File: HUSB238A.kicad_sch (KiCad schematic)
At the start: 1 part

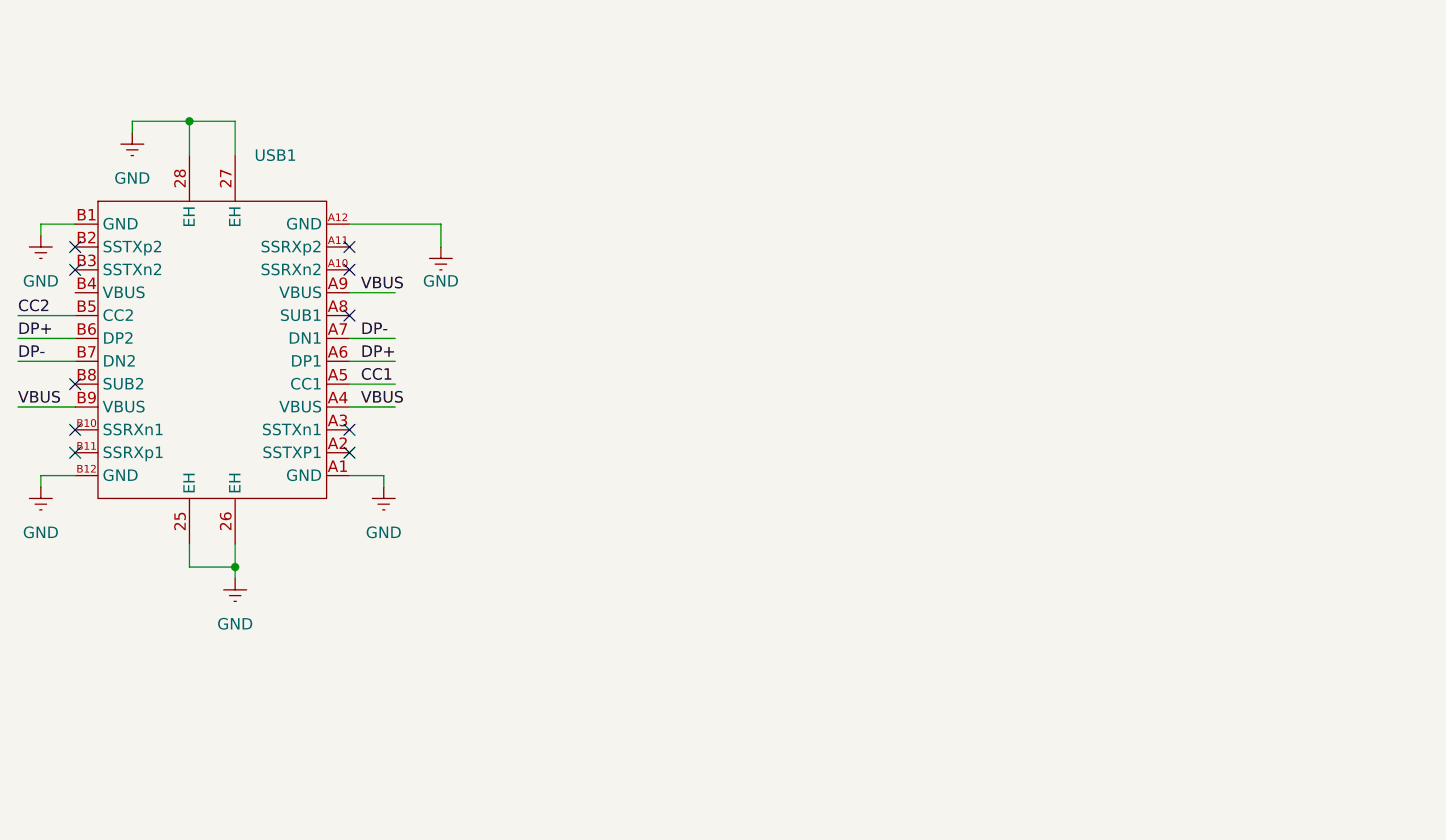
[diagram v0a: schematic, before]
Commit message: add pd power
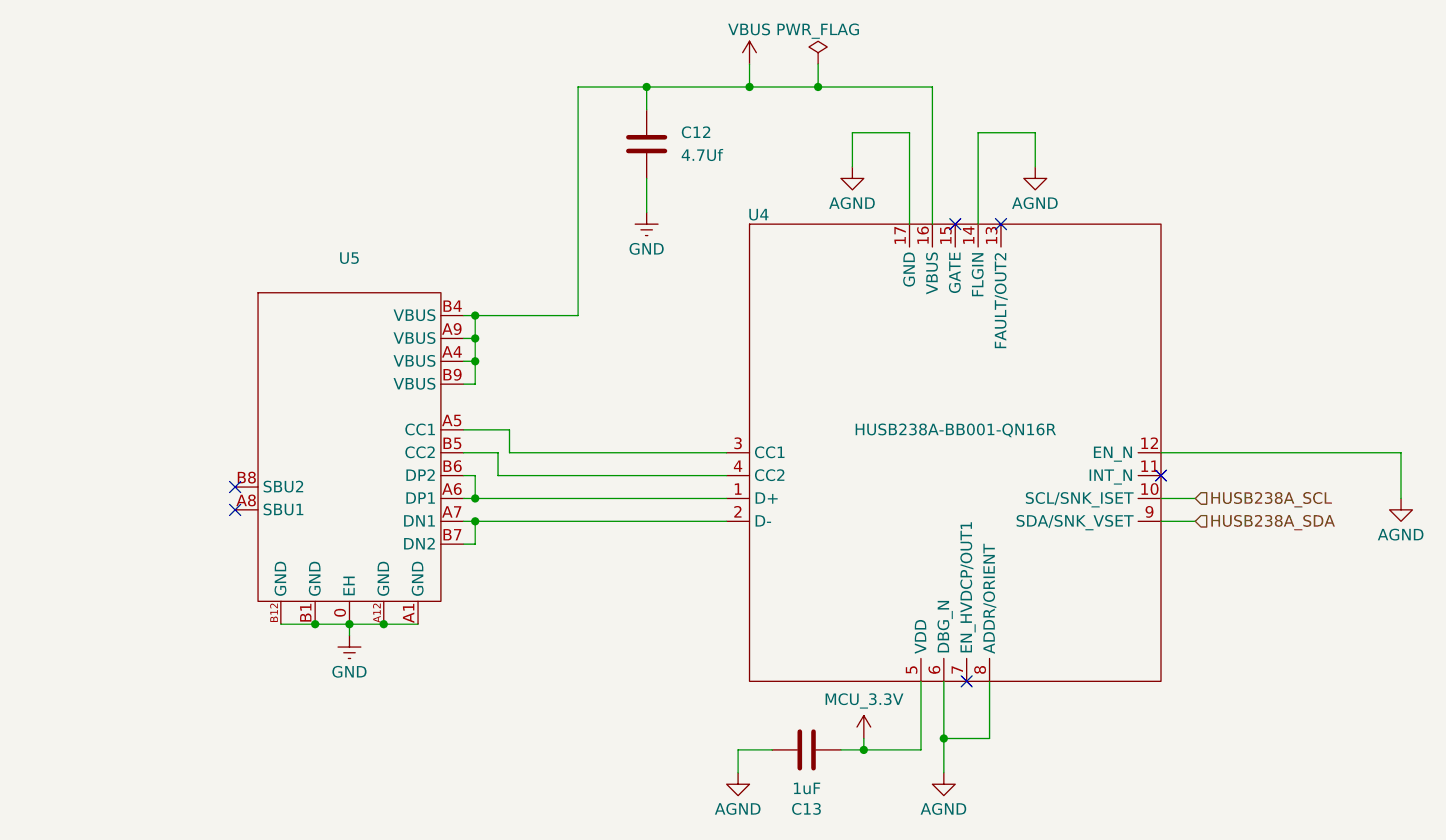
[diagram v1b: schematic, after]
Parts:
- removed USB1: ~, EasyEDA_Lib:USB-C-SMD_U263-241N-4BQC03, symbol EasyEDA_Lib:KH-TYPE-C-L9.3-24P
- added C12: 4.7Uf, symbol Device:C
- added C13: 1uF, symbol Device:C
- added U4: HUSB238A-BB001-QN16R, EasyEDA_Lib:QFN-16_L3.0-W3.0-P0.50-BL-EP1.7, symbol EasyEDA_Lib:HUSB238A-BB001-QN16R
- added U5: ~, EasyEDA_Lib:TYPE-C-SMD_USB4120-03-C, symbol EasyEDA_Lib:TYPE-C 16PLT-H10.0
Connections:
- net GND: now also C12.2, U5.0 (EH), U5.A1 (GND), U5.A12 (GND), U5.B1 (GND), U5.B12 (GND)
- net VBUS: now also C12.1, U4.16 (VBUS), U5.A4 (VBUS), U5.A9 (VBUS), U5.B4 (VBUS), U5.B9 (VBUS)
- new net: U4.3 (CC1), U5.A5 (CC1)
- new net: U4.1 (D+), U5.A6 (DP1), U5.B6 (DP2)
- new net: U4.2 (D-), U5.A7 (DN1), U5.B7 (DN2)
- new net: U4.4 (CC2), U5.B5 (CC2)
- new net AGND: C13.2, U4.12 (EN_N), U4.14 (FLGIN), U4.17 (GND), U4.6 (DBG_N), U4.8 (ADDR/ORIENT)
- new net HUSB238A_SCL: U4.10 (SCL/SNK_ISET)
- new net HUSB238A_SDA: U4.9 (SDA/SNK_VSET)
- new net MCU_3.3V: C13.1, U4.5 (VDD)
- no-connect marks 10 -> 6

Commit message: feat: add as5047p
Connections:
- net MCU_3.3V renamed +3.3V
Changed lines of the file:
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@@
 	)
 	(hierarchical_label "HUSB238A_SCL"
-		(shape input)
+		(shape bidirectional)
 		(at 176.53 107.95 0)
 		(effects
@@
 	)
 	(hierarchical_label "HUSB238A_SDA"
-		(shape input)
+		(shape bidirectional)
 		(at 176.53 110.49 0)
 		(effects
@@
 			)
 		)
-		(property "Value" "MCU_3.3V"
+		(property "Value" "+3.3V"
 			(at 139.7 130.302 0)
 			(effects

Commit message: feat: add can and usart connector
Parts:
- C12: value 4.7Uf -> 4.7u
- C13: value 1uF -> 1u
- U5: value ~ -> TYPE-C 16PLT-H10.0
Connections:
- net AGND is gone; now on net GND: C13.2, U4.12 (EN_N), U4.14 (FLGIN), U4.17 (GND), U4.6 (DBG_N), U4.8 (ADDR/ORIENT)

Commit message: change components
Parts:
- U4, U5: now not fitted
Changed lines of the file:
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@@
 		(in_bom yes)
 		(on_board yes)
-		(dnp no)
+		(dnp yes)
 		(property "Reference" "#PWR017"
 			(at 199.39 114.3 0)
@@
 		(in_bom yes)
 		(on_board yes)
-		(dnp no)
+		(dnp yes)
 		(property "Reference" "#PWR018"
 			(at 158.75 77.47 0)
@@
 		(in_bom yes)
 		(on_board yes)
-		(dnp no)
+		(dnp yes)
 		(fields_autoplaced yes)
 		(property "Reference" "U5"
@@
 		(in_bom yes)
 		(on_board yes)
-		(dnp no)
+		(dnp yes)
 		(property "Reference" "#PWR08"
 			(at 148.59 144.78 0)
@@
 		(in_bom yes)
 		(on_board yes)
-		(dnp no)
+		(dnp yes)
 		(property "Reference" "#FLG02"
 			(at 134.62 57.785 0)
@@
 		(in_bom yes)
 		(on_board yes)
-		(dnp no)
+		(dnp yes)
 		(property "Reference" "#PWR021"
 			(at 127 63.5 0)
@@
 		(in_bom yes)
 		(on_board yes)
-		(dnp no)
+		(dnp yes)
 		(property "Reference" "#PWR019"
 			(at 138.43 77.47 0)
@@
 		(in_bom yes)
 		(on_board yes)
-		(dnp no)
+		(dnp yes)
 		(property "Reference" "#PWR04"
 			(at 125.73 144.78 0)
@@
 		(in_bom yes)
 		(on_board yes)
-		(dnp no)
+		(dnp yes)
 		(property "Reference" "#PWR016"
 			(at 82.55 129.54 0)
@@
 		(in_bom yes)
 		(on_board yes)
-		(dnp no)
+		(dnp yes)
 		(property "Reference" "#PWR024"
 			(at 139.7 138.43 0)
@@
 		(in_bom yes)
 		(on_board yes)
-		(dnp no)
+		(dnp yes)
 		(property "Reference" "#PWR020"
 			(at 115.57 82.55 0)
@@
 		(in_bom yes)
 		(on_board yes)
-		(dnp no)
+		(dnp yes)
 		(fields_autoplaced yes)
 		(property "Reference" "U4"
